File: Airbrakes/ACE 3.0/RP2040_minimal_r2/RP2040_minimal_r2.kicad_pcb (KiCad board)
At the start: 2 copper layers, 52 x 51 mm, 44 parts, among them J1 USB_B_Micro, J2 Conn_01x02, J3 Conn_02x18_Odd_Even, J4 Conn_02x18_Odd_Even, U1 NCP1117-3.3_SOT223, U2 W25Q128JVS, U3 RP2040, U4 BMI088, U5 BMP581, U6 BMM350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

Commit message: small update
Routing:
- net +3V3: track 49.0 -> 48.5 mm
- net GND: track 52.5 -> 52.0 mm
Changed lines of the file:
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@@
-		(net 1)
-	)
-	(segment
-		(start 108.24 118.5)
-		(end 108.24 119)
-		(width 0.15)
-		(layer "F.Cu")
 		(net 1)
 	)
@@
 		(layer "F.Cu")
 		(net 5)
-	)
-	(segment
-		(start 109.59995 118.59995)
-		(end 110 119)
-		(width 0.15)
-		(layer "F.Cu")
-		(net 5)

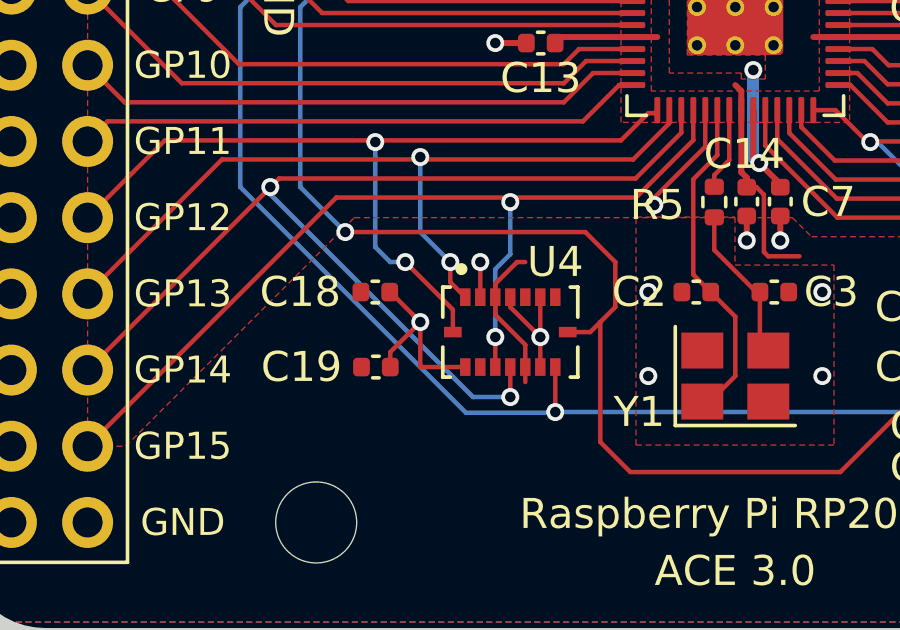
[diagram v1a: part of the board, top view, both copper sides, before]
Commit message: make slight changes to ACE 3.0
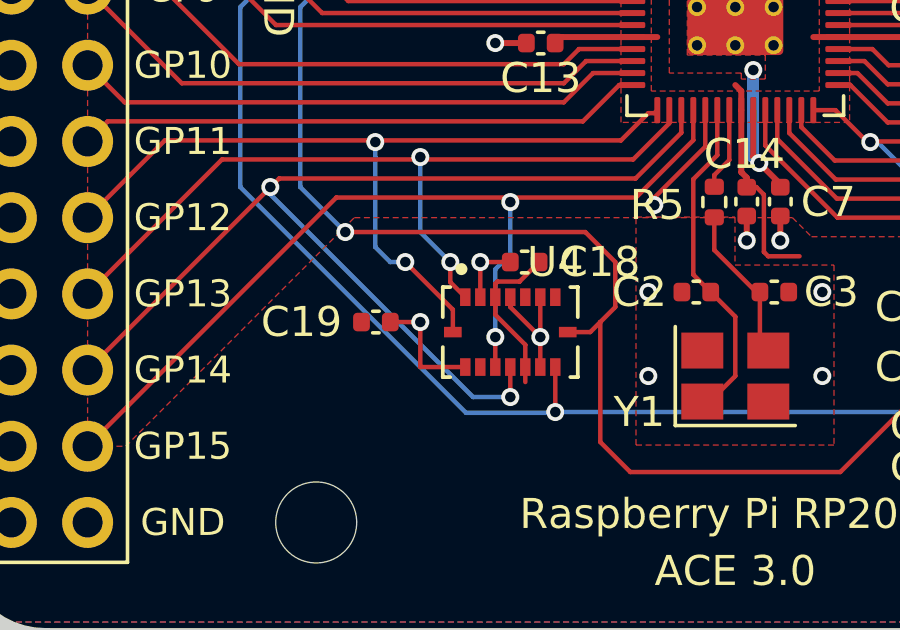
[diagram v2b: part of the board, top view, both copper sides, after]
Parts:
- moved C18 5.08 mm to (93.0, 108.5), turned to 180 degrees
- moved C19 1.50 mm to (88.0, 110.5)
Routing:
- net GND: track 52.0 -> 50.3 mm
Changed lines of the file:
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@@
 	(footprint "Capacitor_SMD:C_0402_1005Metric"
 		(layer "F.Cu")
-		(at 88 109.5)
+		(at 92.98 108.5 180)
 		(descr "Capacitor SMD 0402 (1005 Metric), square (rectangular) end terminal, IPC_7351 nominal, (Body size source: IPC-SM-782 page 76, https://www.pcb-3d.com/wordpress/wp-content/uploads/ipc-sm-782a_amendment_1_and_2.pdf), generated with kicad-footprint-generator")
 		(tags "capacitor")
 		(property "Reference" "C18"
-			(at -2.5 0 0)
+			(at -2.5 0 180)
 			(layer "F.SilkS")
 			(effects
@@
 		)
 		(property "Value" "100n"
-			(at -2 1.16 0)
+			(at -2 1.16 180)
 			(layer "F.Fab")
 			(effects
@@
 		)
 		(property "Footprint" "Capacitor_SMD:C_0402_1005Metric"
-			(at 0 0 0)
+			(at 0 0 180)
 			(unlocked yes)
 			(layer "F.Fab")
@@
 		)
 		(property "Datasheet" ""
-			(at 0 0 0)
+			(at 0 0 180)
 			(unlocked yes)
 			(layer "F.Fab")
@@
 		)
 		(property "Description" ""
-			(at 0 0 0)
+			(at 0 0 180)
 			(unlocked yes)
 			(layer "F.Fab")
@@
 		(attr smd)
 		(fp_line
-			(start -0.107836 -0.36)
-			(end 0.107836 -0.36)
+			(start -0.107836 0.36)
+			(end 0.107836 0.36)
 			(stroke
 				(width 0.12)
@@
 		)
 		(fp_line
-			(start -0.107836 0.36)
-			(end 0.107836 0.36)
+			(start -0.107836 -0.36)
+			(end 0.107836 -0.36)
 			(stroke
 				(width 0.12)
@@
 		)
 		(fp_line
-			(start -0.91 -0.46)
-			(end 0.91 -0.46)
+			(start 0.91 0.46)
+			(end -0.91 0.46)
 			(stroke
 				(width 0.05)
@@
 		)
 		(fp_line
-			(start -0.91 0.46)
-			(end -0.91 -0.46)
+			(start 0.91 -0.46)
+			(end 0.91 0.46)
 			(stroke
 				(width 0.05)
@@
 		)
 		(fp_line
-			(start 0.91 -0.46)
-			(end 0.91 0.46)
+			(start -0.91 0.46)
+			(end -0.91 -0.46)
 			(stroke
 				(width 0.05)
@@
 		)
 		(fp_line
-			(start 0.91 0.46)
-			(end -0.91 0.46)
+			(start -0.91 -0.46)
+			(end 0.91 -0.46)
 			(stroke
 				(width 0.05)
@@
 		)
 		(fp_line
-			(start -0.5 -0.25)
-			(end 0.5 -0.25)
+			(start 0.5 0.25)
+			(end -0.5 0.25)
 			(stroke
 				(width 0.1)
@@
 		)
 		(fp_line
-			(start -0.5 0.25)
-			(end -0.5 -0.25)
+			(start 0.5 -0.25)
+			(end 0.5 0.25)
 			(stroke
 				(width 0.1)
@@
 		)
 		(fp_line
-			(start 0.5 -0.25)
-			(end 0.5 0.25)
+			(start -0.5 0.25)
+			(end -0.5 -0.25)
 			(stroke
 				(width 0.1)
@@
 		)
 		(fp_line
-			(start 0.5 0.25)
-			(end -0.5 0.25)
+			(start -0.5 -0.25)
+			(end 0.5 -0.25)
 			(stroke
 				(width 0.1)
@@
 		)
 		(fp_text user "${REFERENCE}"
-			(at 0 0 0)
+			(at 0 0 180)
 			(layer "F.Fab")
 			(effects
@@
 		)
 		(pad "1" smd roundrect
-			(at -0.48 0)
+			(at -0.48 0 180)
 			(size 0.56 0.62)
 			(layers "F.Cu" "F.Paste" "F.Mask")
@@
 		)
 		(pad "2" smd roundrect
-			(at 0.48 0)
+			(at 0.48 0 180)
 			(size 0.56 0.62)
 			(layers "F.Cu" "F.Paste" "F.Mask")
@@
 	(footprint "Capacitor_SMD:C_0402_1005Metric"
 		(layer "F.Cu")
-		(at 88.02 112)
+		(at 88.02 110.5)
 		(descr "Capacitor SMD 0402 (1005 Metric), square (rectangular) end terminal, IPC_7351 nominal, (Body size source: IPC-SM-782 page 76, https://www.pcb-3d.com/wordpress/wp-content/uploads/ipc-sm-782a_amendment_1_and_2.pdf), generated with kicad-footprint-generator")
 		(tags "capacitor")
@@
 	)
 	(segment
-		(start 88.48 109.5)
-		(end 88.5 109.5)
-		(width 0.15)
-		(layer "F.Cu")
-		(net 1)
-	)
-	(segment
 		(start 112 110.5)
 		(end 111.999999 110)
@@
 	)
 	(segment
-		(start 88.5 112)
-		(end 88.5 111.5)
+		(start 107.17975 115.11975)
+		(end 107.17975 115.17975)
 		(width 0.15)
 		(layer "F.Cu")
@@
 	)
 	(segment
-		(start 107.17975 115.11975)
-		(end 107.17975 115.17975)
+		(start 106.5 118.5)
+		(end 108.24 118.5)
 		(width 0.15)
 		(layer "F.Cu")
@@
 	)
 	(segment
-		(start 106.5 118.5)
-		(end 108.24 118.5)
+		(start 92.5 108.5)
+		(end 91.5 108.5)
 		(width 0.15)
 		(layer "F.Cu")
@@
 	(segment
 		(start 89.5 110.5)
-		(end 89.25 110.25)
+		(end 88.5 110.5)
 		(width 0.15)
 		(layer "F.Cu")
@@
 	)
 	(segment
-		(start 88.5 111.5)
-		(end 89.5 110.5)
-		(width 0.15)
-		(layer "F.Cu")
-		(net 1)
-	)
-	(segment
-		(start 88.5 109.5)
-		(end 89.5 110.5)
-		(width 0.15)
-		(layer "F.Cu")
-		(net 1)
-	)
-	(segment
 		(start 100 92.03)
 		(end 100 91.2)
@@
 	)
 	(segment
-		(start 92 109.225)
-		(end 92.725 108.5)
-		(width 0.15)
-		(layer "F.Cu")
-		(net 5)
-	)
-	(segment
-		(start 92.725 108.5)
-		(end 93 108.5)
-		(width 0.15)
-		(layer "F.Cu")
-		(net 5)
-	)
-	(segment
 		(start 96.5625 101)
 		(end 94.2 101)
@@
 	)
 	(segment
+		(start 92 109.225)
+		(end 92.075 109.15)
+		(width 0.15)
+		(layer "F.Cu")
+		(net 5)
+	)
+	(segment
 		(start 100.2 95.7)
 		(end 100.2 96.5625)
@@
 	)
 	(segment
+		(start 92.075 109.15)
+		(end 92.81 109.15)
+		(width 0.15)
+		(layer "F.Cu")
+		(net 5)
+	)
+	(segment
 		(start 100.701 106)
 		(end 100.9525 106.2515)
@@
 		(width 0.15)
 		(layer "F.Cu")
+		(net 5)
+	)
+	(segment
+		(start 92.81 109.15)
+		(end 93.46 108.5)
+		(width 0.15)
+		(layer "F.Cu")

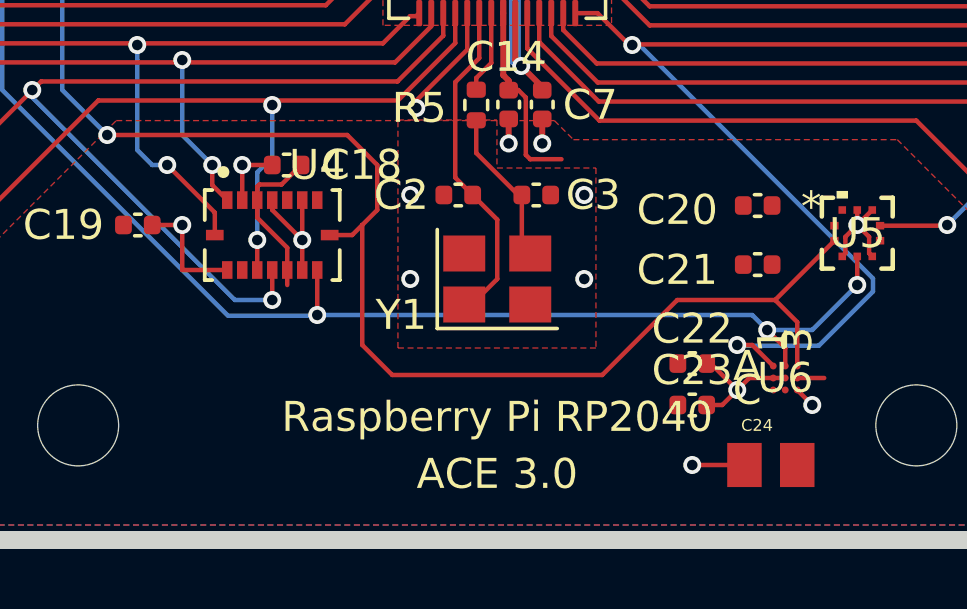
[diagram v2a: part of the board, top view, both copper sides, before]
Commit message: move trace from under crystal oscillator
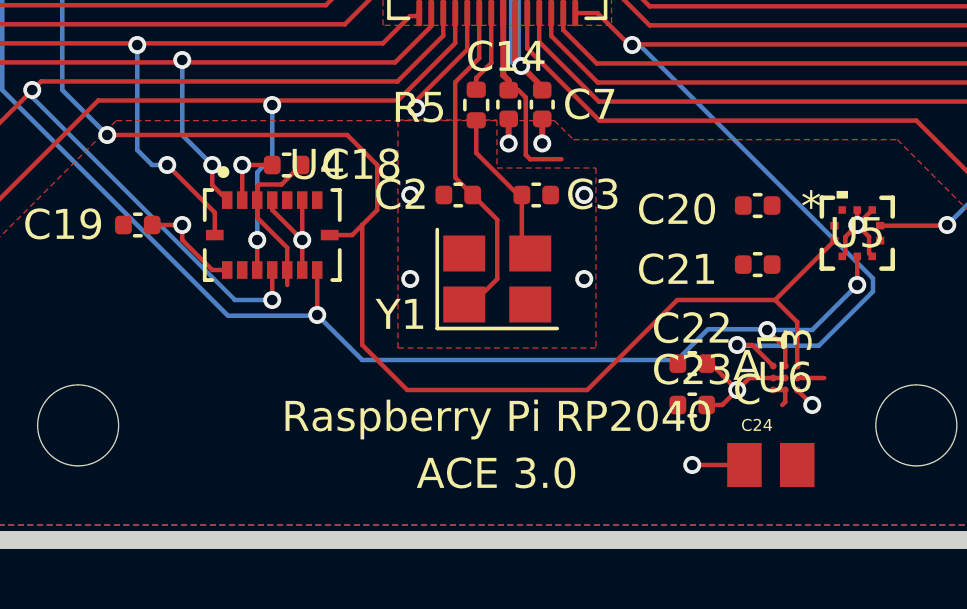
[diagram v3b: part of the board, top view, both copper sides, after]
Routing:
- net +3V3: track 48.9 -> 49.9 mm
- net /SDA: track 71.2 -> 72.0 mm
- net GND: track 50.3 -> 49.7 mm
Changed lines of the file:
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@@
+	)
+	(segment
+		(start 91 112)
+		(end 90.5 112)
+		(width 0.15)
+		(layer "F.Cu")
+		(net 1)
 	)
 	(segment
@@
 	)
 	(segment
+		(start 90.5 112)
+		(end 89.5 111)
+		(width 0.15)
+		(layer "F.Cu")
+		(net 1)
+	)
+	(segment
 		(start 106.97 94.6)
 		(end 108 94.6)
@@
 	)
 	(segment
-		(start 89.5 112)
-		(end 89.5 110.5)
-		(width 0.15)
-		(layer "F.Cu")
-		(net 1)
-	)
-	(segment
 		(start 106.97 96)
 		(end 107.6 96)
@@
 	)
 	(segment
+		(start 89.5 111)
+		(end 89.5 110.5)
+		(width 0.15)
+		(layer "F.Cu")
+		(net 1)
+	)
+	(segment
 		(start 97.3 106.6)
 		(end 97.3 106.3545)
@@
 		(end 102.46 71.45)
 		(width 0.2)
-		(layer "F.Cu")
-		(net 1)
-	)
-	(segment
-		(start 91 112)
-		(end 89.5 112)
-		(width 0.15)
 		(layer "F.Cu")
 		(net 1)
@@
 	)
 	(segment
+		(start 109.1999 116)
+		(end 109.59995 116)
+		(width 0.15)
+		(layer "F.Cu")
+		(net 5)
+	)
+	(segment
 		(start 96.5625 101)
 		(end 94.2 101)
@@
 		(end 100.350001 94.112535)
 		(width 0.2)
+		(layer "F.Cu")
+		(net 5)
+	)
+	(segment
+		(start 109.59995 116.40005)
+		(end 109.5 116.5)
+		(width 0.15)
+		(layer "F.Cu")
+		(net 5)
+	)
+	(segment
+		(start 109.59995 116)
+		(end 109.59995 116.40005)
+		(width 0.15)
 		(layer "F.Cu")
 		(net 5)
@@
 	)
 	(segment
+		(start 107.025 113.975)
+		(end 108.975 113.975)
+		(width 0.15)
+		(layer "B.Cu")
+		(net 54)
+	)
+	(segment
+		(start 94 113.5)
+		(end 95.5 115)
+		(width 0.15)
+		(layer "B.Cu")
+		(net 54)
+	)
+	(segment
 		(start 110.5 114)
 		(end 112 112.5)
@@
 	)
 	(segment
-		(start 94 113.5)
-		(end 108.5 113.5)
+		(start 86 97.5)
+		(end 83.5 100)
 		(width 0.15)
 		(layer "B.Cu")
@@
 	)
 	(segment
-		(start 86 97.5)
-		(end 83.5 100)
+		(start 95.5 115)
+		(end 106 115)
 		(width 0.15)
 		(layer "B.Cu")
@@
 	)
 	(segment
-		(start 108.5 113.5)
+		(start 108.975 113.975)
 		(end 109 114)
 		(width 0.15)
@@
 	)
 	(segment
+		(start 106 115)
+		(end 107.025 113.975)
+		(width 0.15)
+		(layer "B.Cu")
+		(net 54)
+	)
+	(segment
 		(start 83.5 106)
 		(end 91.025 113.525)
@@
 	)
 	(segment
+		(start 106 113)
+		(end 109.262699 113)
+		(width 0.15)
+		(layer "F.Cu")
+		(net 55)
+	)
+	(segment
 		(start 87 107.5)
 		(end 95 107.5)
@@
 	)
 	(segment
-		(start 103.5 115.5)
+		(start 103 116)
 		(end 106 113)
-		(width 0.15)
-		(layer "F.Cu")
-		(net 55)
-	)
-	(segment
-		(start 106 113)
-		(end 109.262699 113)
 		(width 0.15)
 		(layer "F.Cu")
@@
 	)
 	(segment
-		(start 96.5 115.5)
-		(end 103.5 115.5)
-		(width 0.15)
-		(layer "F.Cu")
-		(net 55)
-	)
-	(segment
 		(start 79.68 90.51)
 		(end 78.41 89.24)
@@
 	)
 	(segment
+		(start 95.5 114.5)
+		(end 97 116)
+		(width 0.15)
+		(layer "F.Cu")
+		(net 55)
+	)
+	(segment
 		(start 87.1 99.8)
 		(end 86.5 99.2)
@@
 	)
 	(segment
+		(start 95 107.5)
+		(end 96 108.5)
+		(width 0.15)
+		(layer "F.Cu")
+		(net 55)
+	)
+	(segment
+		(start 109.262699 113)
+		(end 110 113.737301)
+		(width 0.15)
+		(layer "F.Cu")
+		(net 55)
+	)
+	(segment
+		(start 86.3 99)
+		(end 79.68 92.38)
+		(width 0.15)
+		(layer "F.Cu")
+		(net 55)
+	)
+	(segment
+		(start 95.5 110.5)
+		(end 95.165 110.835)
+		(width 0.15)
+		(layer "F.Cu")
+		(net 55)
+	)
+	(segment
+		(start 96 108.5)
+		(end 96 110)
+		(width 0.15)
+		(layer "F.Cu")
+		(net 55)
+	)
+	(segment
+		(start 95.165 110.835)
+		(end 94.415 110.835)
+		(width 0.15)
+		(layer "F.Cu")
+		(net 55)
+	)
+	(segment
+		(start 110 113.737301)
+		(end 110 115.1999)
+		(width 0.15)
+		(layer "F.Cu")
+		(net 55)
+	)
+	(segment
+		(start 79.68 92.38)
+		(end 79.68 90.51)
+		(width 0.15)
+		(layer "F.Cu")
+		(net 55)
+	)
+	(segment
+		(start 97 116)
+		(end 103 116)
+		(width 0.15)
+		(layer "F.Cu")
+		(net 55)
+	)
+	(segment
 		(start 95.5 110.5)
 		(end 95.5 114.5)
 		(width 0.15)
 		(layer "F.Cu")
-		(net 55)
-	)
-	(segment
-		(start 95 107.5)
-		(end 96 108.5)
-		(width 0.15)
-		(layer "F.Cu")
-		(net 55)
-	)
-	(segment
-		(start 109.262699 113)
-		(end 110 113.737301)
-		(width 0.15)
-		(layer "F.Cu")
-		(net 55)
-	)
-	(segment
-		(start 86.3 99)
-		(end 79.68 92.38)
-		(width 0.15)
-		(layer "F.Cu")
-		(net 55)
-	)
-	(segment
-		(start 95.5 110.5)
-		(end 95.165 110.835)
-		(width 0.15)
-		(layer "F.Cu")
-		(net 55)
-	)
-	(segment
-		(start 96 108.5)
-		(end 96 110)
-		(width 0.15)
-		(layer "F.Cu")
-		(net 55)
-	)
-	(segment
-		(start 95.165 110.835)
-		(end 94.415 110.835)
-		(width 0.15)
-		(layer "F.Cu")
-		(net 55)
-	)
-	(segment
-		(start 110 113.737301)
-		(end 110 115.1999)
-		(width 0.15)
-		(layer "F.Cu")
-		(net 55)
-	)
-	(segment
-		(start 95.5 114.5)
-		(end 96.5 115.5)
-		(width 0.15)
-		(layer "F.Cu")
-		(net 55)
-	)
-	(segment
-		(start 79.68 92.38)
-		(end 79.68 90.51)
-		(width 0.15)
-		(layer "F.Cu")

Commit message: fix some labelling on schematic for ACE 3.0
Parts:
- moved C20 3.60 mm to (112.0, 108.5)
- moved C21 1.55 mm to (109.5, 110.5), turned to 90 degrees
- moved C23 0.71 mm to (107.0, 117.0)
- moved C19 0.50 mm to (88.5, 110.5)
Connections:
- J3 pad 12: /GPIO4 -> /SDA
- J3 pad 14: /GPIO5 -> /SCL
- J3 pad 28: /GPIO12 -> /INT1_ACCEL
- J3 pad 30: /GPIO13 -> /INT2_ACCEL
- J3 pad 32: /GPIO14 -> /INT3_GYRO
- J3 pad 34: /GPIO15 -> /INT4_GYRO
- J4 pad 27: /GPIO16 -> /INT_BARO
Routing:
- net GND: track 49.7 -> 51.7 mm, vias 29 -> 30
- net /INT_MAG: track 37.9 -> 39.7 mm
- net +3V3: track 49.9 -> 50.6 mm

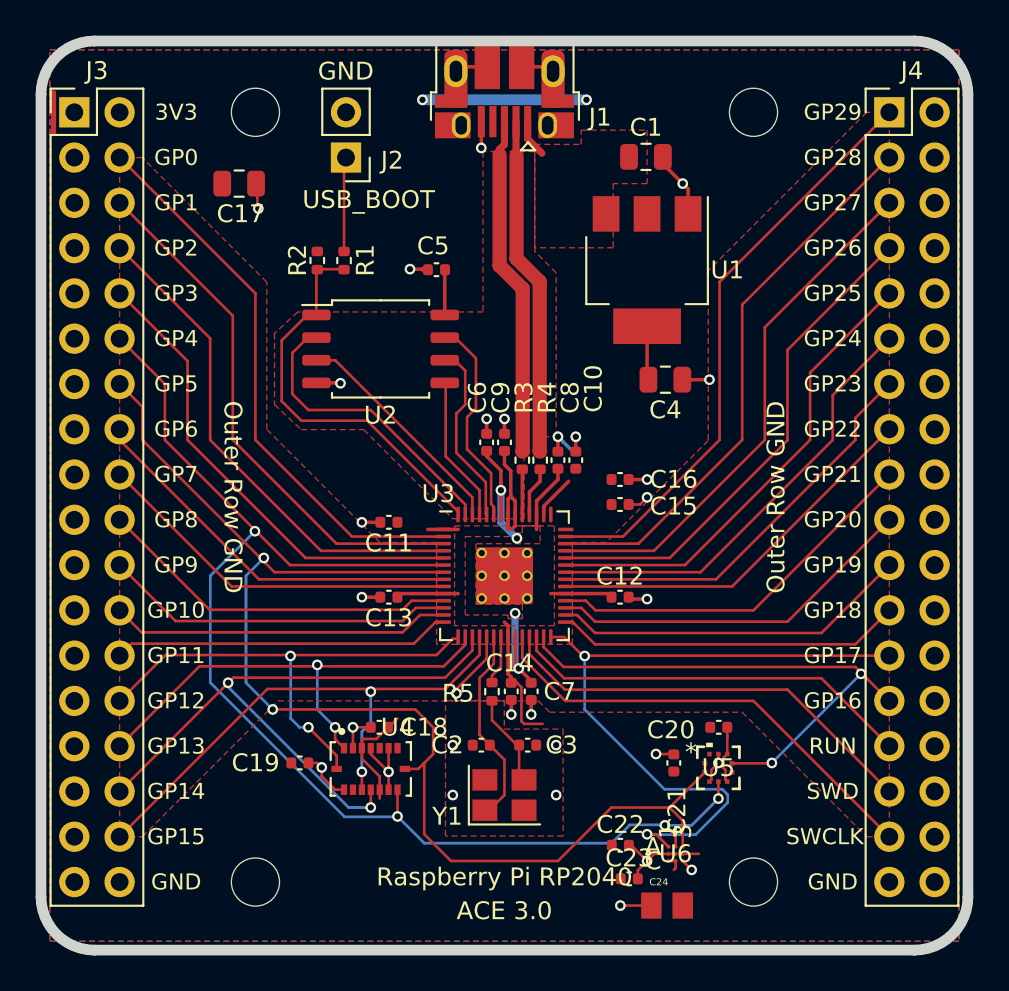
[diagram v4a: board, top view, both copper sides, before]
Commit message: Beginning refactor + add local libraries folder
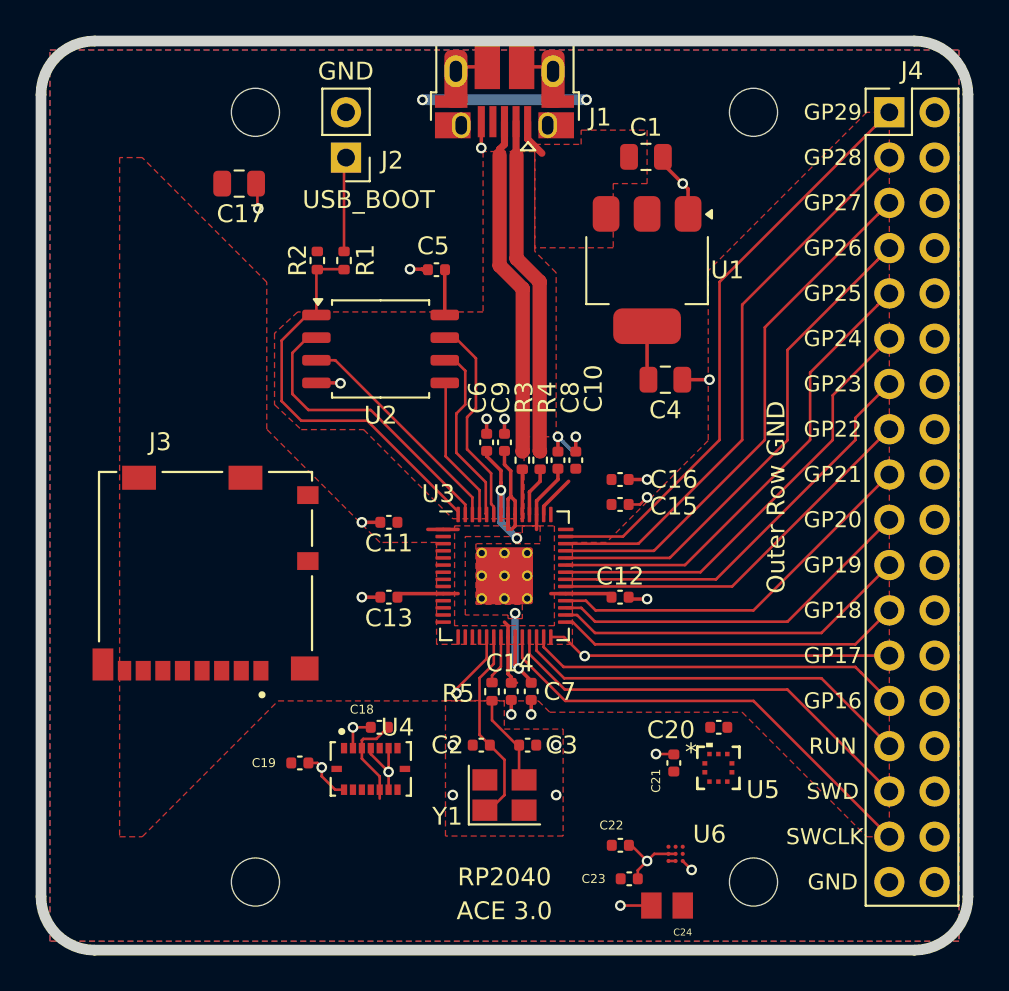
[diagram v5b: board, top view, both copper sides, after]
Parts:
- J3: value Conn_02x18_Odd_Even -> 104031-0811; footprint Connector_PinHeader_2.54mm:PinHeader_2x18_P2.54mm_Vertical -> 1040310811-molex_usb:MOLEX_104031-0811
- moved J3 26.9 mm to (83.2, 99.9)
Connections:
- J3 pad 1: GND -> unconnected-(J3-DAT2-Pad1)
- J3 pad 10: /GPIO3 -> unconnected-(J3-SW-2-Pad10)
- J3 pad 2: +3V3 -> unconnected-(J3-CD/DAT3-Pad2)
- J3 pad 3: GND -> unconnected-(J3-CMD-Pad3)
- J3 pad 4: /GPIO0 -> unconnected-(J3-VDD-Pad4)
- J3 pad 5: GND -> unconnected-(J3-CLK-Pad5)
- J3 pad 6: /GPIO1 -> unconnected-(J3-VSS-Pad6)
- J3 pad 7: GND -> unconnected-(J3-DAT0-Pad7)
- J3 pad 8: /GPIO2 -> unconnected-(J3-DAT1-Pad8)
- J3 pad 9: GND -> unconnected-(J3-SW-1-Pad9)
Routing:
- net /SDA: track 72.0 -> 0.00 mm, vias 4 -> 0
- net /SCL: track 71.0 -> 0.00 mm, vias 2 -> 0
- net /INT3_GYRO: track 35.9 -> 0.00 mm, vias 2 -> 0
- net /GPIO0: track 31.8 -> 0.00 mm
- net /INT4_GYRO: track 31.2 -> 0.00 mm, vias 2 -> 0
- net /GPIO1: track 30.2 -> 0.00 mm
- net /GPIO2: track 28.5 -> 0.00 mm
- net /INT1_ACCEL: track 28.2 -> 0.00 mm, vias 2 -> 0
- net /INT2_ACCEL: track 27.5 -> 0.00 mm, vias 2 -> 0
- net /GPIO3: track 26.9 -> 0.00 mm
- net /GPIO6: track 22.0 -> 0.00 mm
- net /GPIO7: track 20.8 -> 0.00 mm
- net /GPIO8: track 20.5 -> 0.00 mm
- net /INT_MAG: track 39.7 -> 19.4 mm, vias 2 -> 1
- net /GPIO9: track 19.8 -> 0.00 mm
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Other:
- board text added: "RP2040"
- board text removed: "3V3"
- board text removed: "GP0"
- board text removed: "GP1"
- board text removed: "GP10"
- board text removed: "GP11"
- board text removed: "GP12"
- board text removed: "GP13"
- board text removed: "GP14"
- board text removed: "GP15"
- board text removed: "GP2"
- board text removed: "GP3"
- board text removed: "GP4"
- board text removed: "GP5"
- board text removed: "GP6"
- board text removed: "GP7"
- board text removed: "GP8"
- board text removed: "GP9"
- board text removed: "Raspberry Pi RP2040"
